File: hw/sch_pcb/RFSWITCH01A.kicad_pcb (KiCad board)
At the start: 2 copper layers, 40.1 x 40.1 mm, 31 parts, among them J1 HEADER_2x03_PARALLEL, J10 SMA, J11 HEADER_2x01_PARALLEL, J12 HEADER_2x01_PARALLEL, J2 HEADER_2x01_PARALLEL, J3 SMA, J4 SMA, J5 HEADER_2x01_PARALLEL, J6 HEADER_2x01_PARALLEL, J7 HEADER_2x01_PARALLEL, J8 HEADER_2x01_PARALLEL, J9 SMA, M1 HOLE, M2 HOLE, M3 HOLE, M4 HOLE, U1 TPS22945DCKR, U2 SPF5189Z, U3 PE4259, U4 PE4259

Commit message: Edit
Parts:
- moved L2 3.36 mm to (21.5, -27.5)
- moved L3 2.14 mm to (20.8, -20.8), turned to 180 degrees
- moved C3 1.65 mm to (25.8, -30.2)
- moved C4 1.65 mm to (23.2, -30.2)
- moved U2 1.65 mm to (25.1, -24.8)
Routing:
- net Net-(C3-Pad1): track 7.07 -> 8.68 mm
- net /RX/TX_1: track 12.7 -> 13.7 mm
- net Net-(C5-Pad2): track 4.70 -> 3.98 mm
- net GND: vias 224 -> 219

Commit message: Improve layout.
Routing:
- net /SW2_#CTRL: track 18.3 -> 17.2 mm
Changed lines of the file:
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@@
   (via (at 10.541 -15.494) (size 0.4) (drill 0.15) (layers "F.Cu" "B.Cu") (net 2))
   (via (at 20.193 -25.4) (size 0.4) (drill 0.15) (layers "F.Cu" "B.Cu") (net 2))
-  (via (at 21.463 -18.923) (size 0.4) (drill 0.15) (layers "F.Cu" "B.Cu") (net 2))
   (via (at 14.859 -24.003) (size 0.4) (drill 0.15) (layers "F.Cu" "B.Cu") (net 2))
   (via (at 35.306 -21.209) (size 0.4) (drill 0.15) (layers "F.Cu" "B.Cu") (net 2))
@@
   (via (at 24.003 -28.321) (size 0.4) (drill 0.15) (layers "F.Cu" "B.Cu") (net 2))
   (via (at 35.052 -16.256) (size 0.4) (drill 0.15) (layers "F.Cu" "B.Cu") (net 2))
-  (via (at 21.082 -18.288) (size 0.4) (drill 0.15) (layers "F.Cu" "B.Cu") (net 2))
   (via (at 27.432 -28.067) (size 0.4) (drill 0.15) (layers "F.Cu" "B.Cu") (net 2))
   (via (at 33.02 -19.431) (size 0.4) (drill 0.15) (layers "F.Cu" "B.Cu") (net 2))
@@
   (via (at 16.256 -14.351) (size 0.4) (drill 0.15) (layers "F.Cu" "B.Cu") (net 2))
   (via (at 22.225 -19.304) (size 0.4) (drill 0.15) (layers "F.Cu" "B.Cu") (net 2))
+  (via (at 26.72809 -18.271626) (size 0.4) (drill 0.15) (layers "F.Cu" "B.Cu") (net 2))
   (via (at 23.241 -14.478) (size 0.4) (drill 0.15) (layers "F.Cu" "B.Cu") (net 2))
   (via (at 11.176 -29.21) (size 0.4) (drill 0.15) (layers "F.Cu" "B.Cu") (net 2))
@@
   (via (at 30.48 -20.574) (size 0.4) (drill 0.15) (layers "F.Cu" "B.Cu") (net 2))
   (via (at 17.78 -14.986) (size 0.4) (drill 0.15) (layers "F.Cu" "B.Cu") (net 2))
+  (via (at 19.6596 -18.9992) (size 0.4) (drill 0.15) (layers "F.Cu" "B.Cu") (net 2))
+  (via (at 19.6596 -18.0848) (size 0.4) (drill 0.15) (layers "F.Cu" "B.Cu") (net 2))
   (via (at 23.241 -20.828) (size 0.4) (drill 0.15) (layers "F.Cu" "B.Cu") (net 2))
   (via (at 7.62 -13.081) (size 0.4) (drill 0.15) (layers "F.Cu" "B.Cu") (net 2))
@@
   (via (at 33.909 -27.94) (size 0.4) (drill 0.15) (layers "F.Cu" "B.Cu") (net 2))
   (via (at 11.176 -13.589) (size 0.4) (drill 0.15) (layers "F.Cu" "B.Cu") (net 2))
+  (via (at 18.542 -18.0848) (size 0.4) (drill 0.15) (layers "F.Cu" "B.Cu") (net 2))
   (via (at 19.558 -25.4) (size 0.4) (drill 0.15) (layers "F.Cu" "B.Cu") (net 2))
   (via (at 23.876 -21.336) (size 0.4) (drill 0.15) (layers "F.Cu" "B.Cu") (net 2))
-  (via (at 26.67 -18.288) (size 0.4) (drill 0.15) (layers "F.Cu" "B.Cu") (net 2))
   (via (at 24.765 -19.685) (size 0.4) (drill 0.15) (layers "F.Cu" "B.Cu") (net 2))
   (via (at 18.034 -12.192) (size 0.4) (drill 0.15) (layers "F.Cu" "B.Cu") (net 2))
@@
   (via (at 34.163 -16.383) (size 0.4) (drill 0.15) (layers "F.Cu" "B.Cu") (net 2))
   (via (at 13.081 -13.589) (size 0.4) (drill 0.15) (layers "F.Cu" "B.Cu") (net 2))
+  (via (at 21.282552 -19.178977) (size 0.4) (drill 0.15) (layers "F.Cu" "B.Cu") (net 2))
   (via (at 17.145 -19.177) (size 0.4) (drill 0.15) (layers "F.Cu" "B.Cu") (net 2))
   (via (at 35.814 -15.748) (size 0.4) (drill 0.15) (layers "F.Cu" "B.Cu") (net 2))
@@
   (via (at 4.572 -15.113) (size 0.4) (drill 0.15) (layers "F.Cu" "B.Cu") (net 2))
   (via (at 7.239 -27.559) (size 0.4) (drill 0.15) (layers "F.Cu" "B.Cu") (net 2))
-  (via (at 20.447 -18.288) (size 0.4) (drill 0.15) (layers "F.Cu" "B.Cu") (net 2))
   (via (at 28.194 -26.924) (size 0.4) (drill 0.15) (layers "F.Cu" "B.Cu") (net 2))
   (via (at 26.67 -14.224) (size 0.4) (drill 0.15) (layers "F.Cu" "B.Cu") (net 2))
@@
   (via (at 21.463 -22.098) (size 0.4) (drill 0.15) (layers "F.Cu" "B.Cu") (net 2))
   (via (at 30.48 -15.494) (size 0.4) (drill 0.15) (layers "F.Cu" "B.Cu") (net 2))
-  (via (at 19.812 -18.415) (size 0.4) (drill 0.15) (layers "F.Cu" "B.Cu") (net 2))
   (via (at 18.796 -12.192) (size 0.4) (drill 0.15) (layers "F.Cu" "B.Cu") (net 2))
   (via (at 28.194 -25.654) (size 0.4) (drill 0.15) (layers "F.Cu" "B.Cu") (net 2))
-  (via (at 20.066 -19.177) (size 0.4) (drill 0.15) (layers "F.Cu" "B.Cu") (net 2))
+  (via (at 20.7264 -18.1864) (size 0.4) (drill 0.15) (layers "F.Cu" "B.Cu") (net 2))
   (via (at 18.288 -25.4) (size 0.4) (drill 0.15) (layers "F.Cu" "B.Cu") (net 2))
   (via (at 18.923 -25.4) (size 0.4) (drill 0.15) (layers "F.Cu" "B.Cu") (net 2))
@@
   (segment (start 20.64 -15.86) (end 20.625 -15.875) (width 0.4) (layer "B.Cu") (net 11))
   (segment (start 15.24 -14.605) (end 16.1925 -15.5575) (width 0.861) (layer "B.Cu") (net 11))
-  (segment (start 22.225 -18.415) (end 22.225 -14.605) (width 0.4) (layer "F.Cu") (net 12))
-  (segment (start 22.225 -14.605) (end 21.59 -13.97) (width 0.4) (layer "F.Cu") (net 12))
-  (via (at 22.225 -18.415) (size 0.8) (drill 0.4) (layers "F.Cu" "B.Cu") (net 12))
+  (segment (start 21.59 -13.97) (end 21.59 -18.4404) (width 0.4) (layer "F.Cu") (net 12))
+  (via (at 21.59 -18.4404) (size 0.8) (drill 0.4) (layers "F.Cu" "B.Cu") (net 12))
   (via (at 21.59 -13.97) (size 0.8) (drill 0.4) (layers "F.Cu" "B.Cu") (net 12))
-  (segment (start 22.54 -17.16) (end 22.54 -18.1) (width 0.4) (layer "B.Cu") (net 12))
   (segment (start 21.59 -7.62) (end 21.59 -13.97) (width 0.4) (layer "B.Cu") (net 12))
-  (segment (start 22.54 -18.1) (end 22.225 -18.415) (width 0.4) (layer "B.Cu") (net 12))
+  (segment (start 22.54 -17.16) (end 22.54 -17.4904) (width 0.4) (layer "B.Cu") (net 12))
   (segment (start 20.32 -6.35) (end 21.59 -7.62) (width 0.4) (layer "B.Cu") (net 12))
   (segment (start 20.32 -3.81) (end 20.32 -6.35) (width 0.4) (layer "B.Cu") (net 12))
+  (segment (start 22.54 -17.4904) (end 21.59 -18.4404) (width 0.4) (layer "B.Cu") (net 12))
   (segment (start 22.54 -15.86) (end 22.54 -6.67) (width 0.4) (layer "B.Cu") (net 13))
   (segment (start 22.54 -6.67) (end 22.86 -6.35) (width 0.4) (layer "B.Cu") (net 13))
@@
   (segment (start 25.085 -14.92) (end 30.48 -9.525) (width 0.4) (layer "B.Cu") (net 14))
   (segment (start 25.085 -15.86) (end 25.085 -14.92) (width 0.4) (layer "B.Cu") (net 14))
-  (segment (start 25.4 -13.335) (end 25.4 -19.05) (width 0.4) (layer "F.Cu") (net 15))
-  (via (at 25.4 -13.335) (size 0.8) (drill 0.4) (layers "F.Cu" "B.Cu") (net 15))
-  (via (at 25.4 -19.05) (size 0.8) (drill 0.4) (layers "F.Cu" "B.Cu") (net 15))
-  (segment (start 25.085 -18.735) (end 25.4 -19.05) (width 0.4) (layer "B.Cu") (net 15))
-  (segment (start 27.94 -6.35) (end 27.94 -10.795) (width 0.4) (layer "B.Cu") (net 15))
-  (segment (start 27.94 -10.795) (end 25.4 -13.335) (width 0.4) (layer "B.Cu") (net 15))
+  (segment (start 25.9588 -18.4912) (end 25.9588 -17.925515) (width 0.4) (layer "F.Cu") (net 15))
+  (segment (start 25.9588 -17.925515) (end 25.9588 -11.4808) (width 0.4) (layer "F.Cu") (net 15))
+  (via (at 25.9588 -11.4808) (size 0.8) (drill 0.4) (layers "F.Cu" "B.Cu") (net 15))
+  (via (at 25.9588 -18.4912) (size 0.8) (drill 0.4) (layers "F.Cu" "B.Cu") (net 15))
+  (segment (start 27.94 -6.35) (end 25.9588 -8.3312) (width 0.4) (layer "B.Cu") (net 15))
+  (segment (start 25.9588 -8.3312) (end 25.9588 -11.4808) (width 0.4) (layer "B.Cu") (net 15))
+  (segment (start 25.085 -17.16) (end 25.085 -17.6174) (width 0.4) (layer "B.Cu") (net 15))
   (segment (start 27.94 -3.81) (end 27.94 -6.35) (width 0.4) (layer "B.Cu") (net 15))
-  (segment (start 25.085 -17.16) (end 25.085 -18.735) (width 0.4) (layer "B.Cu") (net 15))
+  (segment (start 25.085 -17.6174) (end 25.9588 -18.4912) (width 0.4) (layer "B.Cu") (net 15))
   (segment (start 28.360742 -17.145) (end 27.94 -17.145) (width 0.861) (layer "B.Cu") (net 16))
   (segment (start 28.360742 -17.145) (end 31.535742 -20.32) (width 0.861) (layer "B.Cu") (net 16))
@@
   (segment (start 27 -17.145) (end 27.94 -17.145) (width 0.4) (layer "B.Cu") (net 16))
   (segment (start 34.29 -26.035) (end 34.29 -23.074258) (width 0.861) (layer "B.Cu") (net 16))
-  (segment (start 26.985 -17.16) (end 27 -17.145) (width 0.4) (layer "B.Cu") (net 16))
   (segment (start 31.535742 -20.32) (end 33.147 -20.32) (width 0.861) (layer "B.Cu") (net 16))
   (segment (start 27 -15.875) (end 28.575 -15.875) (width 0.4) (layer "B.Cu") (net 17))

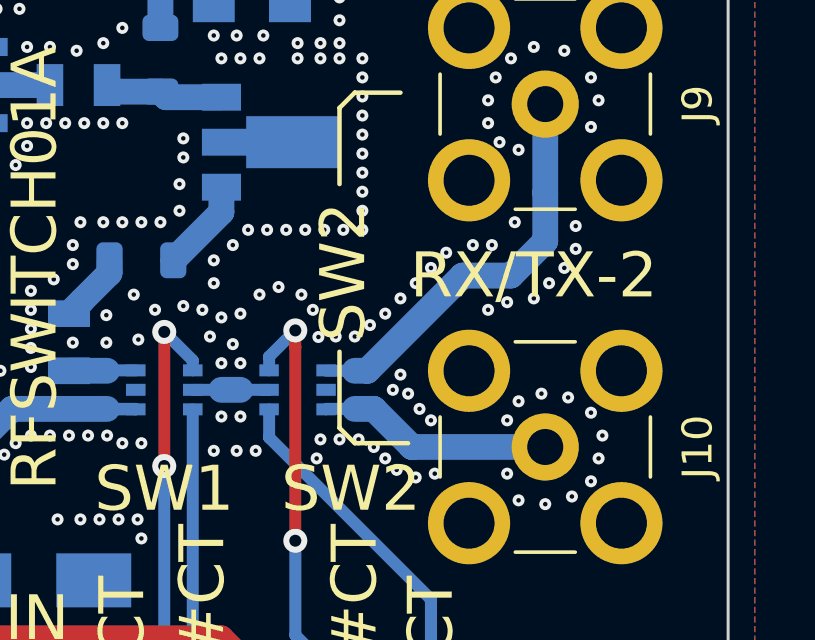
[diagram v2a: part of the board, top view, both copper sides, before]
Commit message: The first experiment with fillet tracks.
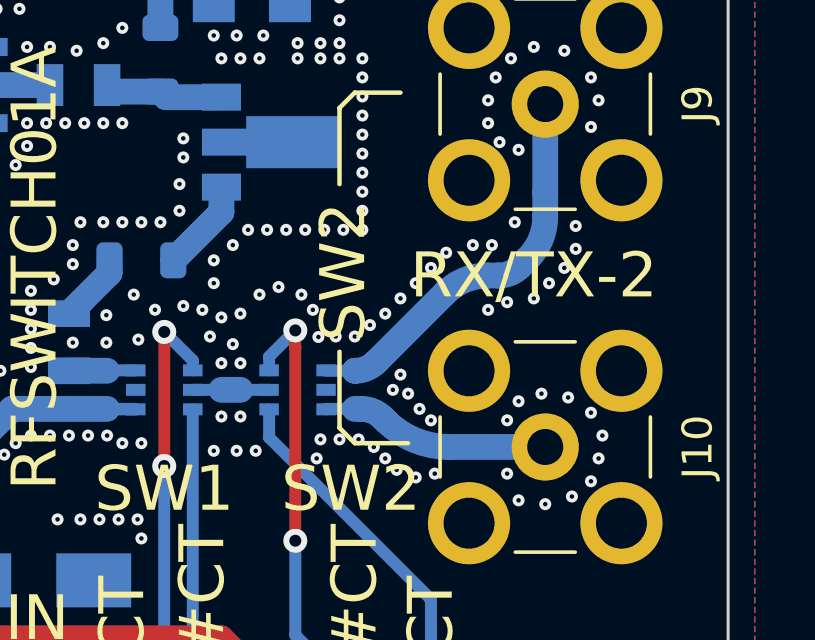
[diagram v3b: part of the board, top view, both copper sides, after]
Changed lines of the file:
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@@
   (segment (start 27.94 -3.81) (end 27.94 -6.35) (width 0.4) (layer "B.Cu") (net 15))
   (segment (start 25.085 -17.6174) (end 25.9588 -18.4912) (width 0.4) (layer "B.Cu") (net 15))
-  (segment (start 28.360742 -17.145) (end 27.94 -17.145) (width 0.861) (layer "B.Cu") (net 16))
-  (segment (start 28.360742 -17.145) (end 31.535742 -20.32) (width 0.861) (layer "B.Cu") (net 16))
-  (segment (start 34.29 -21.463) (end 34.29 -23.074258) (width 0.861) (layer "B.Cu") (net 16))
-  (segment (start 33.147 -20.32) (end 34.29 -21.463) (width 0.861) (layer "B.Cu") (net 16))
+  (segment (start 27.946528 -17.145) (end 27.94 -17.145) (width 0.861) (layer "B.Cu") (net 16))
+  (segment (start 28.653635 -17.437893) (end 30.949955 -19.734213) (width 0.861) (layer "B.Cu") (net 16))
+  (segment (start 34.29 -22.291427) (end 34.29 -23.074258) (width 0.861) (layer "B.Cu") (net 16))
+  (segment (start 33.439893 -20.612893) (end 33.704213 -20.877213) (width 0.861) (layer "B.Cu") (net 16))
   (segment (start 27 -17.145) (end 27.94 -17.145) (width 0.4) (layer "B.Cu") (net 16))
   (segment (start 34.29 -26.035) (end 34.29 -23.074258) (width 0.861) (layer "B.Cu") (net 16))
-  (segment (start 31.535742 -20.32) (end 33.147 -20.32) (width 0.861) (layer "B.Cu") (net 16))
+  (segment (start 32.364169 -20.32) (end 32.732786 -20.32) (width 0.861) (layer "B.Cu") (net 16))
+  (arc (start 30.949955 -19.734213) (mid 31.598802 -20.167759) (end 32.364169 -20.32) (width 0.861) (layer "B.Cu") (net 16))
+  (arc (start 33.439893 -20.612893) (mid 33.11547 -20.39612) (end 32.732786 -20.32) (width 0.861) (layer "B.Cu") (net 16))
+  (arc (start 27.946528 -17.145) (mid 28.329211 -17.22112) (end 28.653635 -17.437893) (width 0.861) (layer "B.Cu") (net 16))
+  (arc (start 34.29 -22.291427) (mid 34.137759 -21.52606) (end 33.704213 -20.877213) (width 0.861) (layer "B.Cu") (net 16))
   (segment (start 27 -15.875) (end 28.575 -15.875) (width 0.4) (layer "B.Cu") (net 17))
   (segment (start 26.985 -15.86) (end 27 -15.875) (width 0.4) (layer "B.Cu") (net 17))
-  (segment (start 28.575 -15.875) (end 27.94 -15.875) (width 0.861) (layer "B.Cu") (net 17))
-  (segment (start 34.29 -14.605) (end 29.845 -14.605) (width 0.861) (layer "B.Cu") (net 17))
-  (segment (start 29.845 -14.605) (end 28.575 -15.875) (width 0.861) (layer "B.Cu") (net 17))
+  (segment (start 28.160786 -15.875) (end 27.94 -15.875) (width 0.861) (layer "B.Cu") (net 17))
+  (segment (start 34.29 -14.605) (end 31.087641 -14.605) (width 0.861) (layer "B.Cu") (net 17))
+  (segment (start 28.966321 -15.483679) (end 28.867893 -15.582107) (width 0.861) (layer "B.Cu") (net 17))
+  (arc (start 28.160786 -15.875) (mid 28.543469 -15.79888) (end 28.867893 -15.582107) (width 0.861) (layer "B.Cu") (net 17))
+  (arc (start 31.087641 -14.605) (mid 29.939591 -14.833361) (end 28.966321 -15.483679) (width 0.861) (layer "B.Cu") (net 17))
   (segment (start 21.27 -33.97) (end 21.27 -36.18) (width 0.4) (layer "B.Cu") (net 18))
   (segment (start 16.675001 -32.854999) (end 20.154999 -32.854999) (width 0.4) (layer "B.Cu") (net 18))
